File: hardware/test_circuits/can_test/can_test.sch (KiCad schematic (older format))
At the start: 37 parts, among them J101 Conn_01x05_Female, SW101 SW_SPDT, SW102 CAN1_RST, SW103 SW_Push, SW104 SW_Push, U101 L7805, U102 MCP2562-E-P, U103 MCP2515-xSO, U104 PIC18F4620-IP, Y101 40MHz, Y102 10MHz

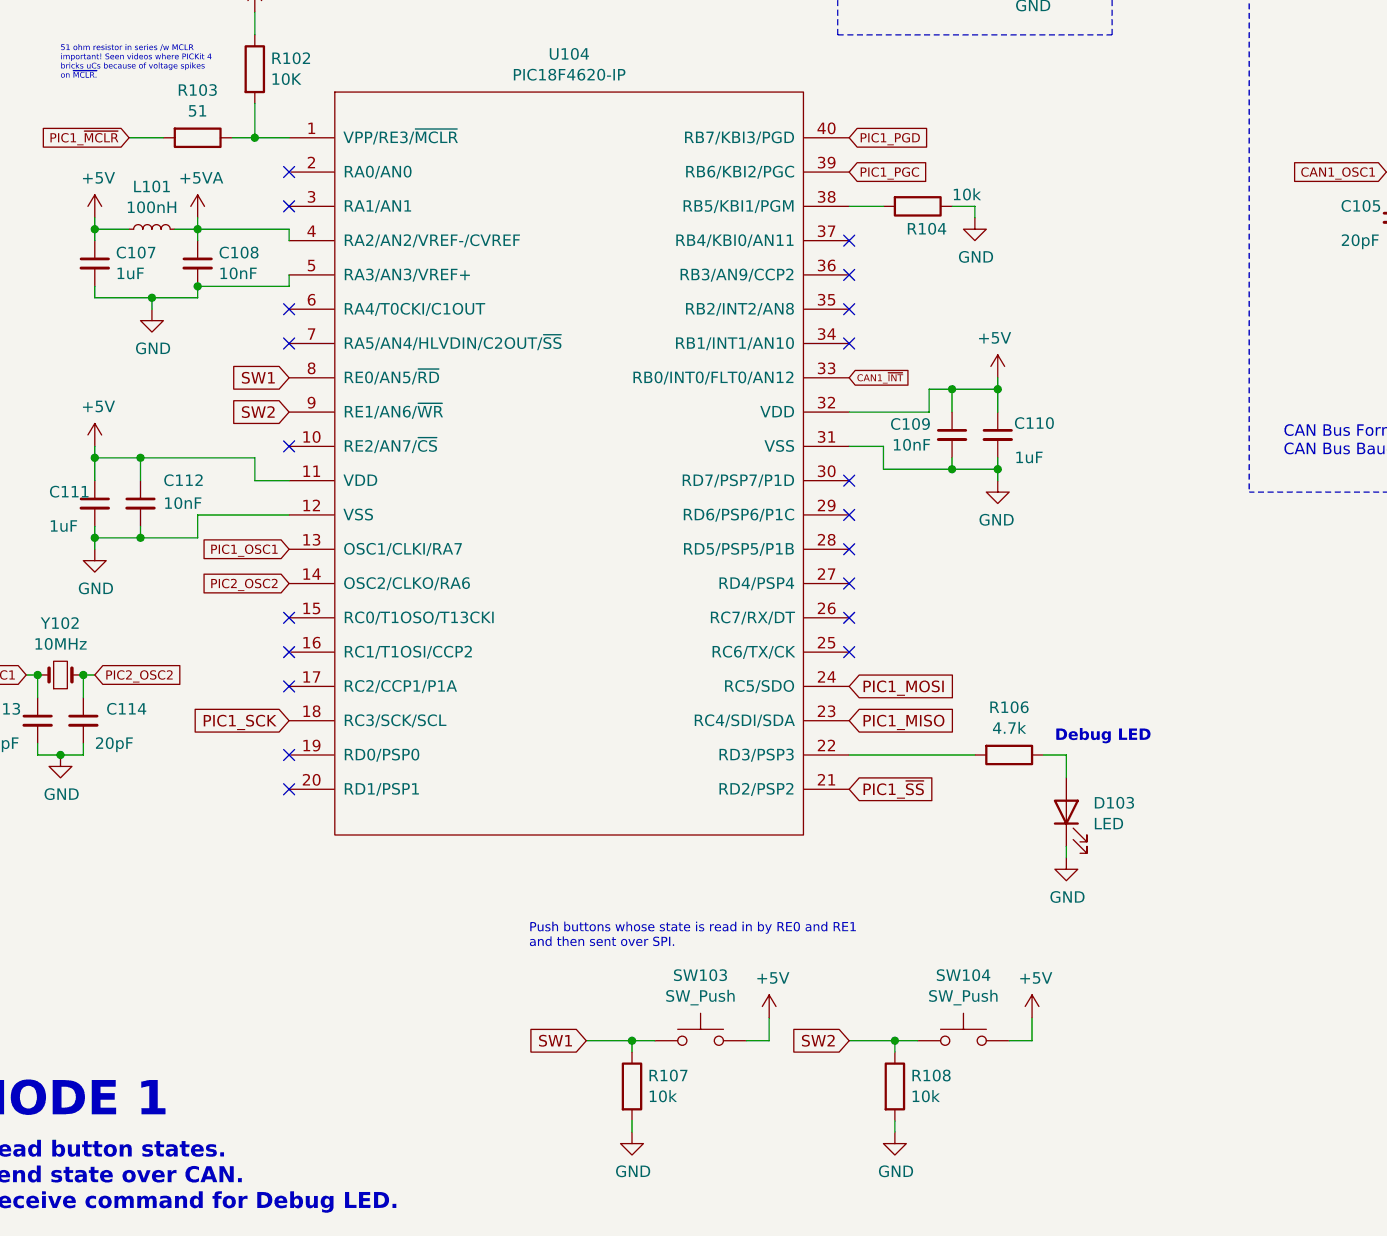
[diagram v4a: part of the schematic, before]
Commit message: Added in a potentiometer for Node 1 to act as an Engine Speed Signal' to drive the point of this project a little more...
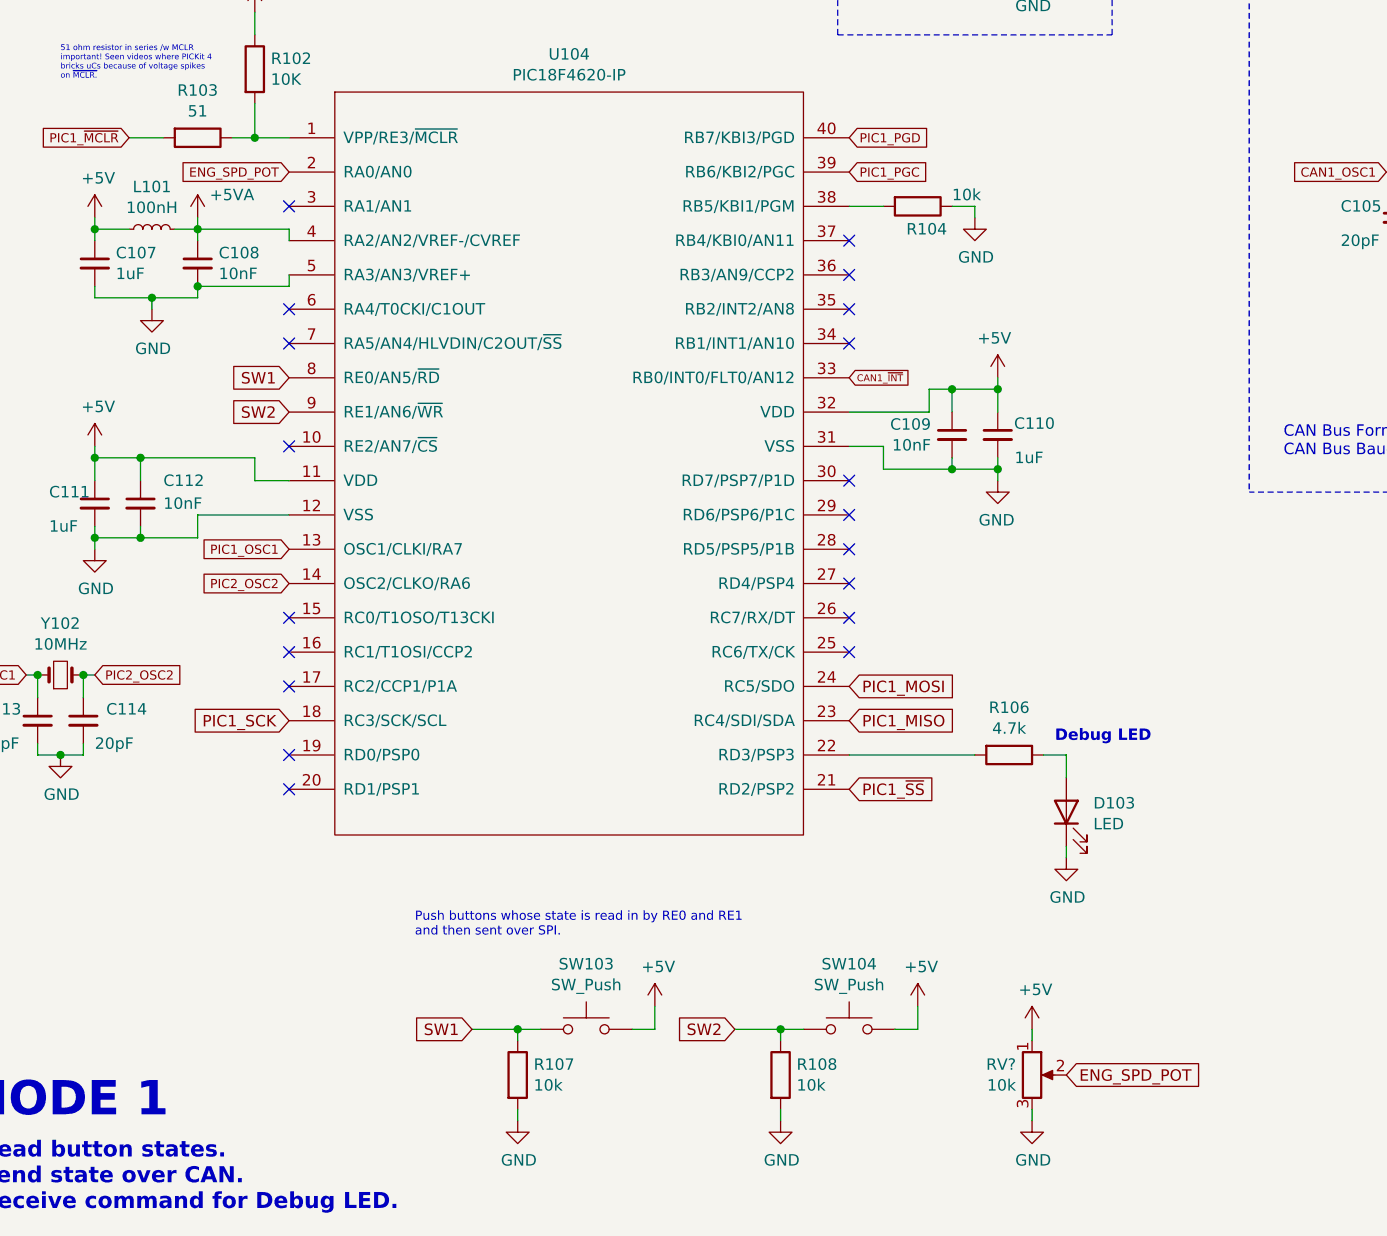
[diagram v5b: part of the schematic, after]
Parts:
- added RV?: 10k, symbol Device:R_POT
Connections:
- net +5V: now also RV?.1
- net GND: now also RV?.3
- net ENG_SPD_POT: now reaches U104.2 (RA0/AN0)
- net ENG_SPD_POT: now also RV?.2
- no-connect marks 24 -> 23
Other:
- moved on the sheet: R107, R108, SW103, SW104
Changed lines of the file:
@@
 Comp ""
 Comment1 "and update the debug LED state through CAN messages."
-Comment2 "This CAN Node will send the state of the two button switches"
+Comment2 "This CAN Node will send the state of the two button switches and the engine speed pot"
 Comment3 ""
 Comment4 "Author: Abdullah Almosalami"
@@
 Text Notes 1150 2500 0    25   ~ 0
 51 ohm resistor in series /w MCLR\nimportant! Seen videos where PICKit 4\nbricks uCs because of voltage spikes\non ~MCLR.
-NoConn ~ 2150 2900
 NoConn ~ 2150 3050
 $Comp
@@
 P 1750 3100
 F 0 "#PWR0120" H 1750 2950 50  0001 C CNN
-F 1 "+5VA" H 1765 3273 50  0000 C CNN
+F 1 "+5VA" H 1900 3200 50  0000 C CNN
 F 2 "" H 1750 3100 50  0001 C CNN
 F 3 "" H 1750 3100 50  0001 C CNN
@@
 L power:+5V #PWR0133
 U 1 1 6187E0DD
-P 5400 6600
-F 0 "#PWR0133" H 5400 6450 50  0001 C CNN
-F 1 "+5V" H 5415 6773 50  0000 C CNN
-F 2 "" H 5400 6600 50  0001 C CNN
-F 3 "" H 5400 6600 50  0001 C CNN
-	1    5400 6600
-	1    0    0    -1
-$EndComp
-Wire Wire Line
-	5400 6700 5400 6600
-Wire Wire Line
-	5300 6700 5400 6700
-Wire Wire Line
-	4800 7100 4800 7050
-Wire Wire Line
-	4800 6700 4900 6700
-Wire Wire Line
-	4800 6750 4800 6700
-Connection ~ 4800 6700
-Wire Wire Line
-	4600 6700 4800 6700
+P 4900 6550
+F 0 "#PWR0133" H 4900 6400 50  0001 C CNN
+F 1 "+5V" H 4915 6723 50  0000 C CNN
+F 2 "" H 4900 6550 50  0001 C CNN
+F 3 "" H 4900 6550 50  0001 C CNN
+	1    4900 6550
+	1    0    0    -1
+$EndComp
+Wire Wire Line
+	4900 6650 4900 6550
+Wire Wire Line
+	4800 6650 4900 6650
+Wire Wire Line
+	4300 7050 4300 7000
+Wire Wire Line
+	4300 6650 4400 6650
+Wire Wire Line
+	4300 6700 4300 6650
+Connection ~ 4300 6650
+Wire Wire Line
+	4100 6650 4300 6650
 $Comp
 L Switch:SW_Push SW104
 U 1 1 6187D56B
-P 5100 6700
-F 0 "SW104" H 5100 6985 50  0000 C CNN
-F 1 "SW_Push" H 5100 6894 50  0000 C CNN
-F 2 "" H 5100 6900 50  0001 C CNN
-F 3 "~" H 5100 6900 50  0001 C CNN
-	1    5100 6700
+P 4600 6650
+F 0 "SW104" H 4600 6935 50  0000 C CNN
+F 1 "SW_Push" H 4600 6844 50  0000 C CNN
+F 2 "" H 4600 6850 50  0001 C CNN
+F 3 "~" H 4600 6850 50  0001 C CNN
+	1    4600 6650
 	1    0    0    -1
 $EndComp
@@
 L power:GND #PWR0135
 U 1 1 6187CD54
-P 4800 7100
-F 0 "#PWR0135" H 4800 6850 50  0001 C CNN
-F 1 "GND" H 4805 6927 50  0000 C CNN
-F 2 "" H 4800 7100 50  0001 C CNN
-F 3 "" H 4800 7100 50  0001 C CNN
-	1    4800 7100
-	1    0    0    -1
-$EndComp
-Text GLabel 4600 6700 0    50   Input ~ 0
+P 4300 7050
+F 0 "#PWR0135" H 4300 6800 50  0001 C CNN
+F 1 "GND" H 4305 6877 50  0000 C CNN
+F 2 "" H 4300 7050 50  0001 C CNN
+F 3 "" H 4300 7050 50  0001 C CNN
+	1    4300 7050
+	1    0    0    -1
+$EndComp
+Text GLabel 4100 6650 0    50   Input ~ 0
 SW2
 $Comp
 L Device:R R108
 U 1 1 618502FD
-P 4800 6900
-F 0 "R108" H 4870 6946 50  0000 L CNN
-F 1 "10k" H 4870 6855 50  0000 L CNN
-F 2 "" V 4730 6900 50  0001 C CNN
-F 3 "~" H 4800 6900 50  0001 C CNN
-	1    4800 6900
+P 4300 6850
+F 0 "R108" H 4370 6896 50  0000 L CNN
+F 1 "10k" H 4370 6805 50  0000 L CNN
+F 2 "" V 4230 6850 50  0001 C CNN
+F 3 "~" H 4300 6850 50  0001 C CNN
+	1    4300 6850
 	1    0    0    -1
 $EndComp
@@
 L power:+5V #PWR0132
 U 1 1 618892F2
-P 4250 6600
-F 0 "#PWR0132" H 4250 6450 50  0001 C CNN
-F 1 "+5V" H 4265 6773 50  0000 C CNN
-F 2 "" H 4250 6600 50  0001 C CNN
-F 3 "" H 4250 6600 50  0001 C CNN
-	1    4250 6600
-	1    0    0    -1
-$EndComp
-Wire Wire Line
-	4250 6700 4250 6600
-Wire Wire Line
-	4150 6700 4250 6700
-Wire Wire Line
-	3650 7100 3650 7050
-Wire Wire Line
-	3650 6700 3750 6700
-Wire Wire Line
-	3650 6750 3650 6700
-Connection ~ 3650 6700
-Wire Wire Line
-	3450 6700 3650 6700
+P 3750 6550
+F 0 "#PWR0132" H 3750 6400 50  0001 C CNN
+F 1 "+5V" H 3765 6723 50  0000 C CNN
+F 2 "" H 3750 6550 50  0001 C CNN
+F 3 "" H 3750 6550 50  0001 C CNN
+	1    3750 6550
+	1    0    0    -1
+$EndComp
+Wire Wire Line
+	3750 6650 3750 6550
+Wire Wire Line
+	3650 6650 3750 6650
+Wire Wire Line
+	3150 7050 3150 7000
+Wire Wire Line
+	3150 6650 3250 6650
+Wire Wire Line
+	3150 6700 3150 6650
+Connection ~ 3150 6650
+Wire Wire Line
+	2950 6650 3150 6650
 $Comp
 L Switch:SW_Push SW103
 U 1 1 61889585
-P 3950 6700
-F 0 "SW103" H 3950 6985 50  0000 C CNN
-F 1 "SW_Push" H 3950 6894 50  0000 C CNN
-F 2 "" H 3950 6900 50  0001 C CNN
-F 3 "~" H 3950 6900 50  0001 C CNN
-	1    3950 6700
+P 3450 6650
+F 0 "SW103" H 3450 6935 50  0000 C CNN
+F 1 "SW_Push" H 3450 6844 50  0000 C CNN
+F 2 "" H 3450 6850 50  0001 C CNN
+F 3 "~" H 3450 6850 50  0001 C CNN
+	1    3450 6650
 	1    0    0    -1
 $EndComp
@@
 L power:GND #PWR0134
 U 1 1 6188958F
-P 3650 7100
-F 0 "#PWR0134" H 3650 6850 50  0001 C CNN
-F 1 "GND" H 3655 6927 50  0000 C CNN
-F 2 "" H 3650 7100 50  0001 C CNN
-F 3 "" H 3650 7100 50  0001 C CNN
-	1    3650 7100
-	1    0    0    -1
-$EndComp
-Text GLabel 3450 6700 0    50   Input ~ 0
+P 3150 7050
+F 0 "#PWR0134" H 3150 6800 50  0001 C CNN
+F 1 "GND" H 3155 6877 50  0000 C CNN
+F 2 "" H 3150 7050 50  0001 C CNN
+F 3 "" H 3150 7050 50  0001 C CNN
+	1    3150 7050
+	1    0    0    -1
+$EndComp
+Text GLabel 2950 6650 0    50   Input ~ 0
 SW1
 $Comp
 L Device:R R107
 U 1 1 6188959A
-P 3650 6900
-F 0 "R107" H 3720 6946 50  0000 L CNN
-F 1 "10k" H 3720 6855 50  0000 L CNN
-F 2 "" V 3580 6900 50  0001 C CNN
-F 3 "~" H 3650 6900 50  0001 C CNN
-	1    3650 6900
-	1    0    0    -1
-$EndComp
-Text Notes 3200 6300 0    40   ~ 0
+P 3150 6850
+F 0 "R107" H 3220 6896 50  0000 L CNN
+F 1 "10k" H 3220 6805 50  0000 L CNN
+F 2 "" V 3080 6850 50  0001 C CNN
+F 3 "~" H 3150 6850 50  0001 C CNN
+	1    3150 6850
+	1    0    0    -1
+$EndComp
+Text Notes 2700 6250 0    40   ~ 0
 Push buttons whose state is read in by RE0 and RE1\nand then sent over SPI.
 NoConn ~ 2150 4100
@@
 NoConn ~ 8950 2600
 NoConn ~ 8950 2500
+$Comp
+L Device:R_POT RV?
+U 1 1 6193C443
+P 5400 6850
+F 0 "RV?" H 5330 6896 50  0000 R CNN
+F 1 "10k" H 5330 6805 50  0000 R CNN
+F 2 "" H 5400 6850 50  0001 C CNN
+F 3 "~" H 5400 6850 50  0001 C CNN
+	1    5400 6850
+	1    0    0    -1
+$EndComp
+$Comp
+L power:+5V #PWR?
+U 1 1 61944396
+P 5400 6650
+F 0 "#PWR?" H 5400 6500 50  0001 C CNN
+F 1 "+5V" H 5415 6823 50  0000 C CNN
+F 2 "" H 5400 6650 50  0001 C CNN
+F 3 "" H 5400 6650 50  0001 C CNN
+	1    5400 6650
+	1    0    0    -1
+$EndComp
+$Comp
+L power:GND #PWR?
+U 1 1 619445F0
+P 5400 7050
+F 0 "#PWR?" H 5400 6800 50  0001 C CNN
+F 1 "GND" H 5405 6877 50  0000 C CNN
+F 2 "" H 5400 7050 50  0001 C CNN
+F 3 "" H 5400 7050 50  0001 C CNN
+	1    5400 7050
+	1    0    0    -1
+$EndComp
+Wire Wire Line
+	5400 6650 5400 6700
+Wire Wire Line
+	5400 7050 5400 7000
+Text GLabel 5550 6850 2    50   Input ~ 0
+ENG_SPD_POT
+Text GLabel 2150 2900 0    40   Input ~ 0
+ENG_SPD_POT
 $EndSCHEMATC

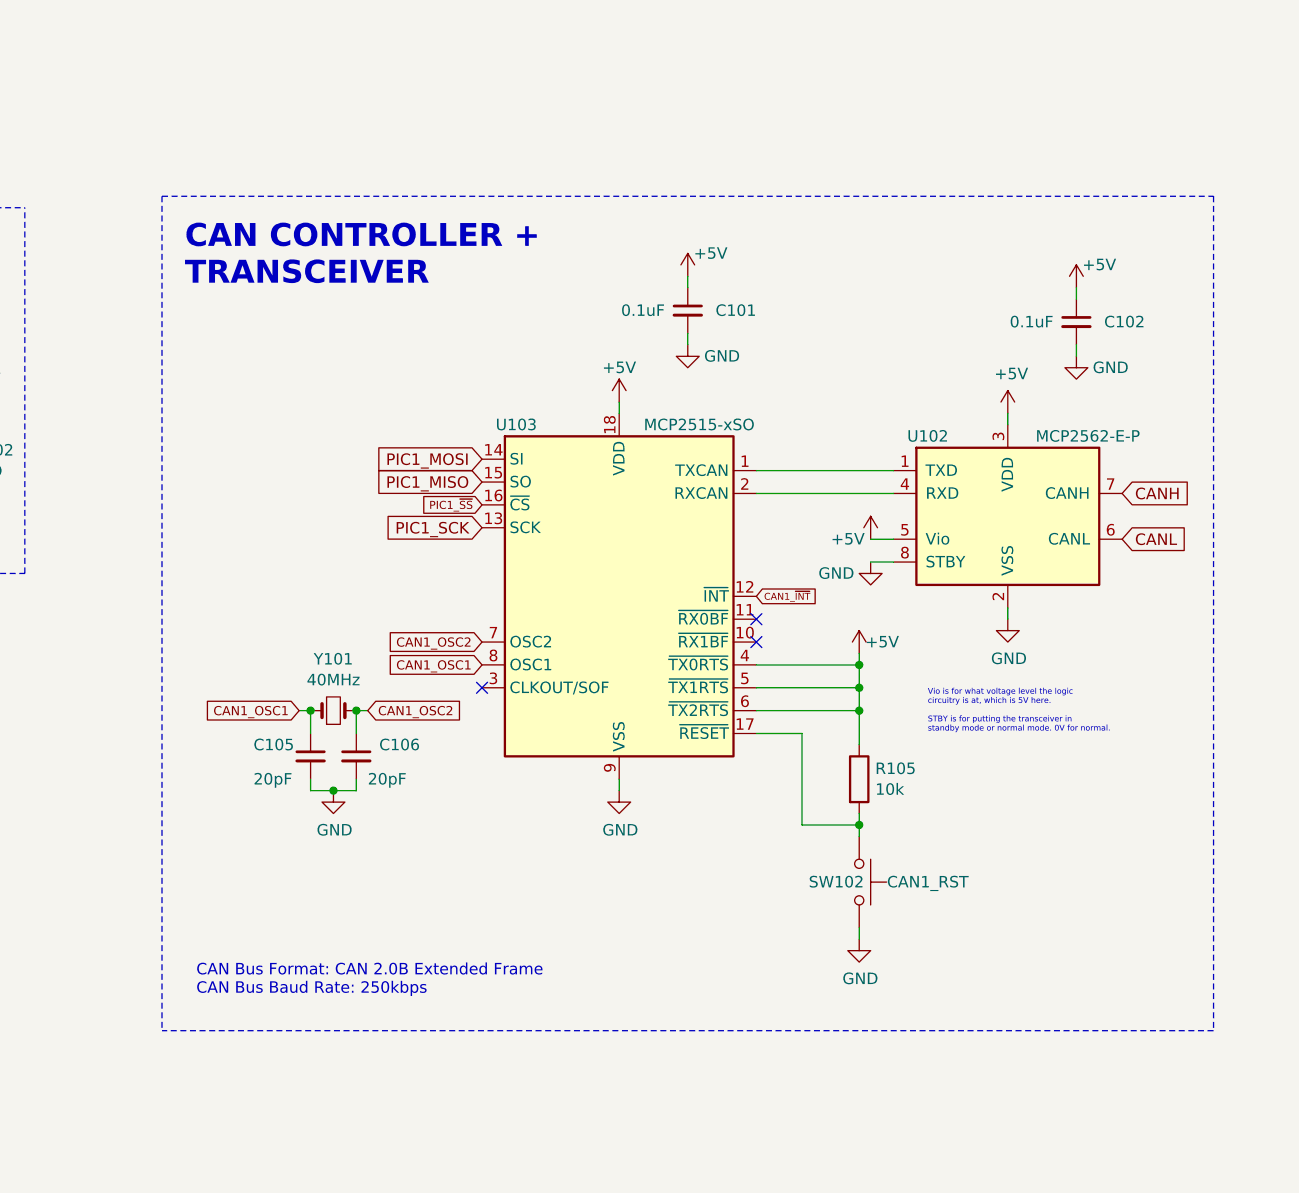
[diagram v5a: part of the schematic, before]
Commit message: Freaken forgot 120ohm termination resistors on the CANH and CANL lines! Doi!
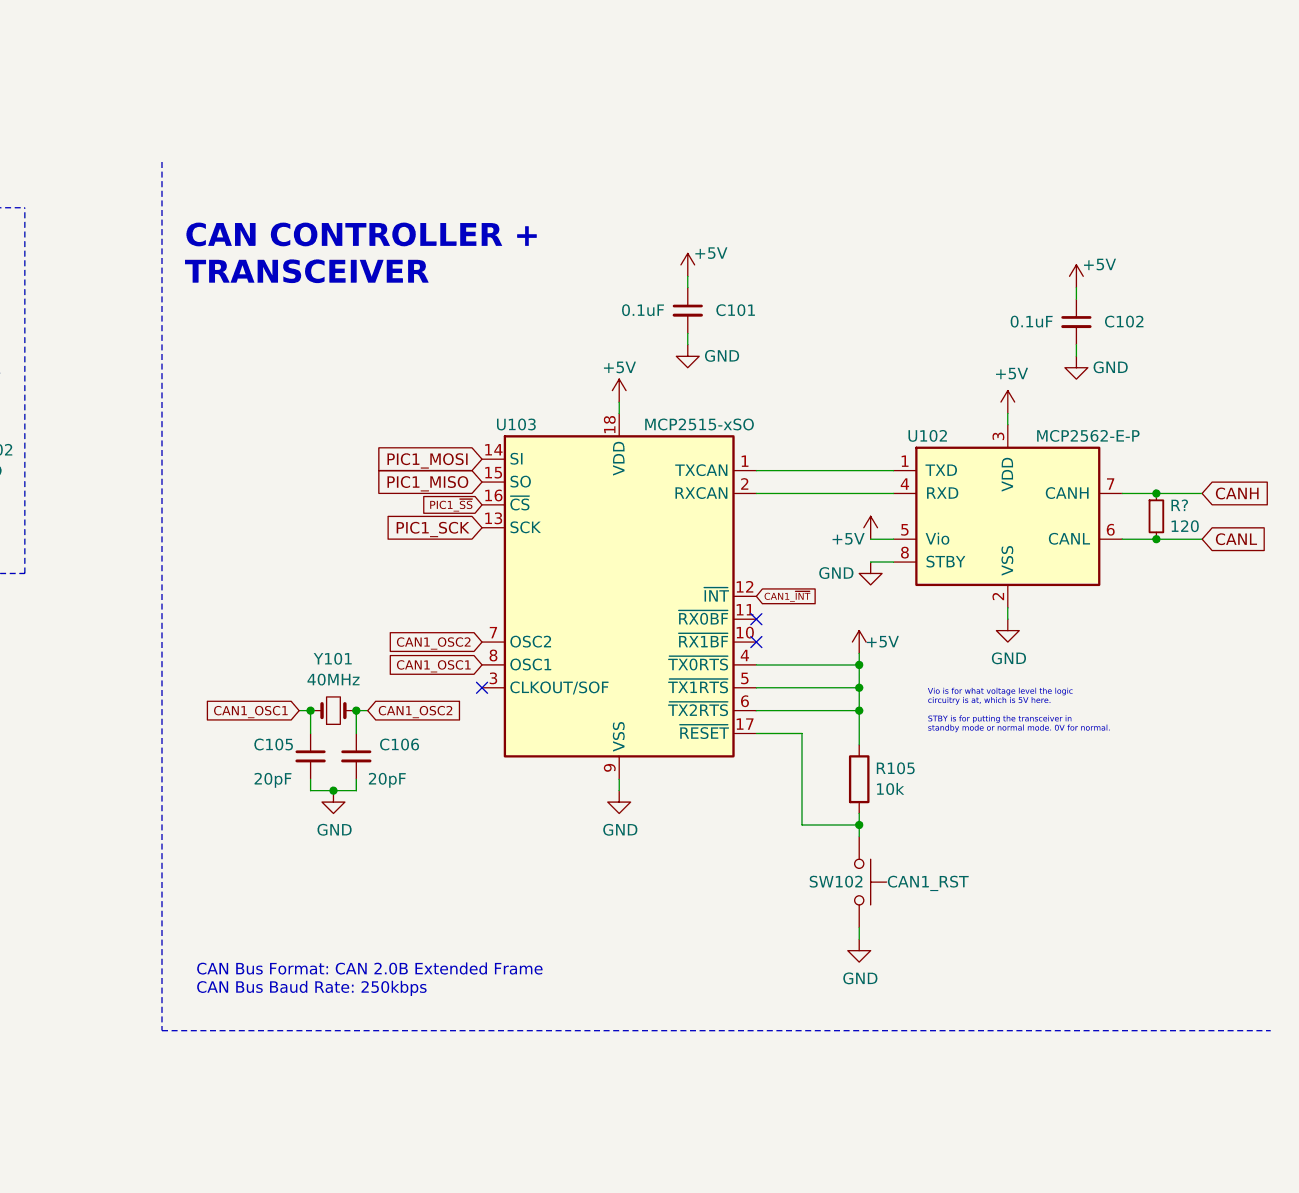
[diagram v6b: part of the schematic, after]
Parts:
- added R?: 120, symbol Device:R_Small
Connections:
- net CANH: now also R?.1
- net CANL: now also R?.2
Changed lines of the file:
@@
 Text Notes 9700 3000 0    25   ~ 0
 Vio is for what voltage level the logic\ncircuitry is at, which is 5V here.\n\nSTBY is for putting the transceiver in\nstandby mode or normal mode. 0V for normal.
-Text GLabel 10550 1950 2    50   Input ~ 0
+Text GLabel 10900 1950 2    50   Input ~ 0
 CANH
-Text GLabel 10550 2150 2    50   Input ~ 0
+Text GLabel 10900 2150 2    50   Input ~ 0
 CANL
-Wire Notes Line
-	6350 650  10950 650
-Wire Notes Line
-	10950 650  10950 4300
-Wire Notes Line
-	10950 4300 6350 4300
-Wire Notes Line
-	6350 650  6350 4300
 Text Notes 6450 1050 0    100  ~ 20
 CAN CONTROLLER +\nTRANSCEIVER
@@
 Text GLabel 2150 2900 0    40   Input ~ 0
 ENG_SPD_POT
+$Comp
+L Device:R_Small R?
+U 1 1 6193BA87
+P 10700 2050
+F 0 "R?" H 10759 2096 50  0000 L CNN
+F 1 "120" H 10759 2005 50  0000 L CNN
+F 2 "" H 10700 2050 50  0001 C CNN
+F 3 "~" H 10700 2050 50  0001 C CNN
+	1    10700 2050
+	1    0    0    -1
+$EndComp
+Wire Wire Line
+	10550 2150 10700 2150
+Connection ~ 10700 2150
+Wire Wire Line
+	10700 2150 10900 2150
+Wire Wire Line
+	10900 1950 10700 1950
+Connection ~ 10700 1950
+Wire Wire Line
+	10700 1950 10550 1950
+Wire Notes Line
+	6350 4300 11200 4300
+Wire Notes Line
+	6350 500  6350 4300
 $EndSCHEMATC
